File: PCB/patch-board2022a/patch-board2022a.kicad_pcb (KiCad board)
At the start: 2 copper layers, 230 x 63 mm, 120 parts, among them J1 USB_B, J10 SERVO POWER SUPPLY, J11 AOUT1, J12 AOUT2, J13 AOUT3, J14 AOUT4, J15 AOUT5, J16 AOUT6, J17 AOUT7, J18 AOUT8, J2 LOGIC POWER SUPPLY, J21 DIGITAL OUT1, J22 DIGITAL OUT2, J23 DIGITAL OUT3, J24 DIGITAL OUT4, J3 MEGA_13-8, J31 S01, J32 S02, J33 S03, J34 S04, J35 S05, J36 S06, J37 S07, J38 S08, J39 S09, J4 MEGA_7-0, J41 SV, J42 SV, J43 SV, J44 SV, J45 SV, J46 SV, J5 MEGA_14-21, J6 MEGA_A8-A15, J7 MEGA_A0-A7, J8 MEGA_POWER, J9 MEGA_22-53, SW1 D1A, SW11 SW_DPST, SW12 SW_DPST, SW13 Conn_01x02, SW2 D1B, SW3 D2A, SW4 D2B, SW5 D3A, SW6 D3B, SW7 D4A, SW8 D4B, U1 74HC00, U10 74HC08, U11 74HC00, U12 74HC08, U13 74HC08, U14 TLP785, U15 TLP785, U16 TLP785, U17 TLP785, U18 TLP785, U19 TLP785, U2 74HC08, U3 74HC08, U4 74HC00, U5 74HC08, U6 74HC08, U7 74HC14, U8 74HC00, U9 74HC08

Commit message: 一応完成
git-svn-id: https://shiro-home.ddns.net/svn/project/motor-driver/trunk@40 73406841-da20-4056-b287-c5b29fcc9b8e
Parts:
- removed J39: S09, Connector_PinHeader_2.54mm:PinHeader_1x03_P2.54mm_Vertical
- J11, J12, J13, J14, J15, J16, J17, J18: footprint Connector_PinHeader_2.54mm:PinHeader_1x02_P2.54mm_Vertical -> Connector_PinHeader_2.54mm:PinHeader_1x03_P2.54mm_Vertical
- J21: value DIGITAL OUT1 -> DOUT1; footprint Connector_PinHeader_2.54mm:PinHeader_1x02_P2.54mm_Vertical -> Connector_PinHeader_2.54mm:PinHeader_1x03_P2.54mm_Vertical
- J22: value DIGITAL OUT2 -> DOUT2; footprint Connector_PinHeader_2.54mm:PinHeader_1x02_P2.54mm_Vertical -> Connector_PinHeader_2.54mm:PinHeader_1x03_P2.54mm_Vertical
- J23: value DIGITAL OUT3 -> DOUT3; footprint Connector_PinHeader_2.54mm:PinHeader_1x02_P2.54mm_Vertical -> Connector_PinHeader_2.54mm:PinHeader_1x03_P2.54mm_Vertical
- J24: value DIGITAL OUT4 -> DOUT4; footprint Connector_PinHeader_2.54mm:PinHeader_1x02_P2.54mm_Vertical -> Connector_PinHeader_2.54mm:PinHeader_1x03_P2.54mm_Vertical
- moved R10 48.3 mm to (151.3, 69.5), turned to 0 degrees
- moved R9 43.3 mm to (151.3, 67.0), turned to 0 degrees
- moved R8 38.6 mm to (151.3, 64.4), turned to 0 degrees
- moved R7 34.2 mm to (151.3, 61.9), turned to 0 degrees
- moved R6 30.2 mm to (151.3, 59.4), turned to 0 degrees
- moved R5 26.8 mm to (151.3, 56.8), turned to 0 degrees
- moved R11 11.4 mm to (125.9, 82.2)
- moved R12 11.4 mm to (120.8, 82.2)
- moved R13 11.4 mm to (115.7, 82.2)
- moved R14 11.4 mm to (110.6, 82.2)
- moved R15 11.4 mm to (105.6, 82.2)
- moved R16 11.4 mm to (100.5, 82.2)
- moved U14 11.4 mm to (128.4, 61.9)
- moved U15 11.4 mm to (123.3, 61.9)
- moved U16 11.4 mm to (118.3, 61.9)
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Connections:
- J11 pad 2: /AOUT1A -> /AOUT1M
- J12 pad 2: /AOUT2A -> /AOUT2M
- J13 pad 2: /AOUT3A -> /AOUT3M
- J14 pad 2: /AOUT4A -> /AOUT4M
- J15 pad 2: /AOUT5A -> /AOUT5M
- J16 pad 2: /AOUT6A -> /AOUT6M
- J17 pad 2: /AOUT7A -> /AOUT7M
- J18 pad 2: /AOUT8A -> /AOUT8M
- J21 pad 1: /DOUT1A -> /DOUT1B
- J21 pad 2: /DOUT1B -> /DOUT1M
- J22 pad 1: /DOUT2A -> /DOUT2B
- J22 pad 2: /DOUT2B -> /DOUT2M
- J23 pad 1: /DOUT3A -> /DOUT3B
- J23 pad 2: /DOUT3B -> /DOUT3M
- J24 pad 1: /DOUT4A -> /DOUT4B
- J24 pad 2: /DOUT4B -> /DOUT4M
- J6 pad 1: Net-(J6-Pad1) -> /SENSOR1
- J6 pad 2: Net-(J6-Pad2) -> /SENSOR2
- J6 pad 3: Net-(J6-Pad3) -> /SENSOR3
- J6 pad 4: Net-(J6-Pad4) -> /SENSOR4
- J6 pad 5: Net-(J6-Pad5) -> /SENSOR5
- J6 pad 6: Net-(J6-Pad6) -> /SENSOR6
- J6 pad 7: Net-(J6-Pad7) -> /SENSOR7
- J6 pad 8: Net-(J6-Pad8) -> /SENSOR8
- J7 pad 1: Net-(J7-Pad1) -> /AOUT8M
- J7 pad 2: Net-(J7-Pad2) -> /AOUT7M
- J7 pad 3: Net-(J7-Pad3) -> /AOUT6M
- J7 pad 4: Net-(J7-Pad4) -> /AOUT5M
- J7 pad 5: Net-(J7-Pad5) -> /AOUT4M
- J7 pad 6: Net-(J7-Pad6) -> /AOUT3M
- J7 pad 7: Net-(J7-Pad7) -> /AOUT2M
- J7 pad 8: Net-(J7-Pad8) -> /AOUT1M
- J9 pad 10: /SENSOR8 -> /LED1
- J9 pad 11: /SENSOR3 -> /SV3IN
- J9 pad 12: /SENSOR9 -> /DIN1A
- J9 pad 13: /SENSOR4 -> /SV4IN
- J9 pad 14: /DIN1A -> /DIN1B
- J9 pad 15: /SENSOR5 -> /SV5IN
- J9 pad 16: /DIN1B -> /DIN2A
- J9 pad 17: /SENSOR6 -> /SV6IN
- J9 pad 18: /DIN2A -> /DIN2B
- J9 pad 19: /SV1IN -> Net-(J9-Pad19)
- J9 pad 20: /DIN2B -> /DIN3A
- J9 pad 21: /SV2IN -> Net-(J9-Pad21)
- J9 pad 22: /DIN3A -> /DIN3B
- J9 pad 23: /SV3IN -> Net-(J9-Pad23)
- J9 pad 24: /DIN3B -> /DIN4A
- J9 pad 25: /SV4IN -> Net-(J9-Pad25)
- J9 pad 26: /DIN4A -> /DIN4B
- J9 pad 27: /SV5IN -> Net-(J9-Pad27)
- J9 pad 28: /DIN4B -> /DOUT3M
- J9 pad 29: /SV6IN -> Net-(J9-Pad29)
- J9 pad 30: Net-(J9-Pad30) -> /DOUT4M
- J9 pad 5: /LED1 -> /SW12
- J9 pad 6: /SW12 -> /DOUT1M
- J9 pad 7: /SENSOR1 -> /SV1IN
- J9 pad 8: /SENSOR7 -> /DOUT2M
- J9 pad 9: /SENSOR2 -> /SV2IN
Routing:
- net /DOUT3M: track 0.00 -> 133.2 mm
- net /DOUT4M: track 0.00 -> 132.1 mm
- net /AOUT1M: track 0.00 -> 128.4 mm, vias 0 -> 2
- net /AOUT2M: track 0.00 -> 118.4 mm, vias 0 -> 2
- net /AOUT4M: track 0.00 -> 116.4 mm, vias 0 -> 2
- net /AOUT3M: track 0.00 -> 114.0 mm, vias 0 -> 2
- net /DOUT1M: track 0.00 -> 108.7 mm
- net /DOUT2M: track 0.00 -> 108.5 mm
- net GND: track 104.5 -> 2.58 mm, vias 34 -> 144
- net /AOUT5M: track 0.00 -> 75.9 mm
- net /SV6IN: track 74.7 -> 3.17 mm
- net /SV5IN: track 67.8 -> 3.17 mm
- net /AOUT6M: track 0.00 -> 62.6 mm
- net /SV4IN: track 60.9 -> 3.17 mm
- net /LED1: track 0.00 -> 54.1 mm, vias 0 -> 3
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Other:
- board text added: "1 28"
- board text added: "2 30"
- board text added: "3 32"
- board text added: "4 34"
- board text added: "5 36"
- board text added: "6 38"
- board text removed: "1 19"
- board text removed: "2 21"
- board text removed: "3 23"
- board text removed: "4 25"
- board text removed: "5 27"
- board text removed: "6 29"
- board text removed: "9 30"

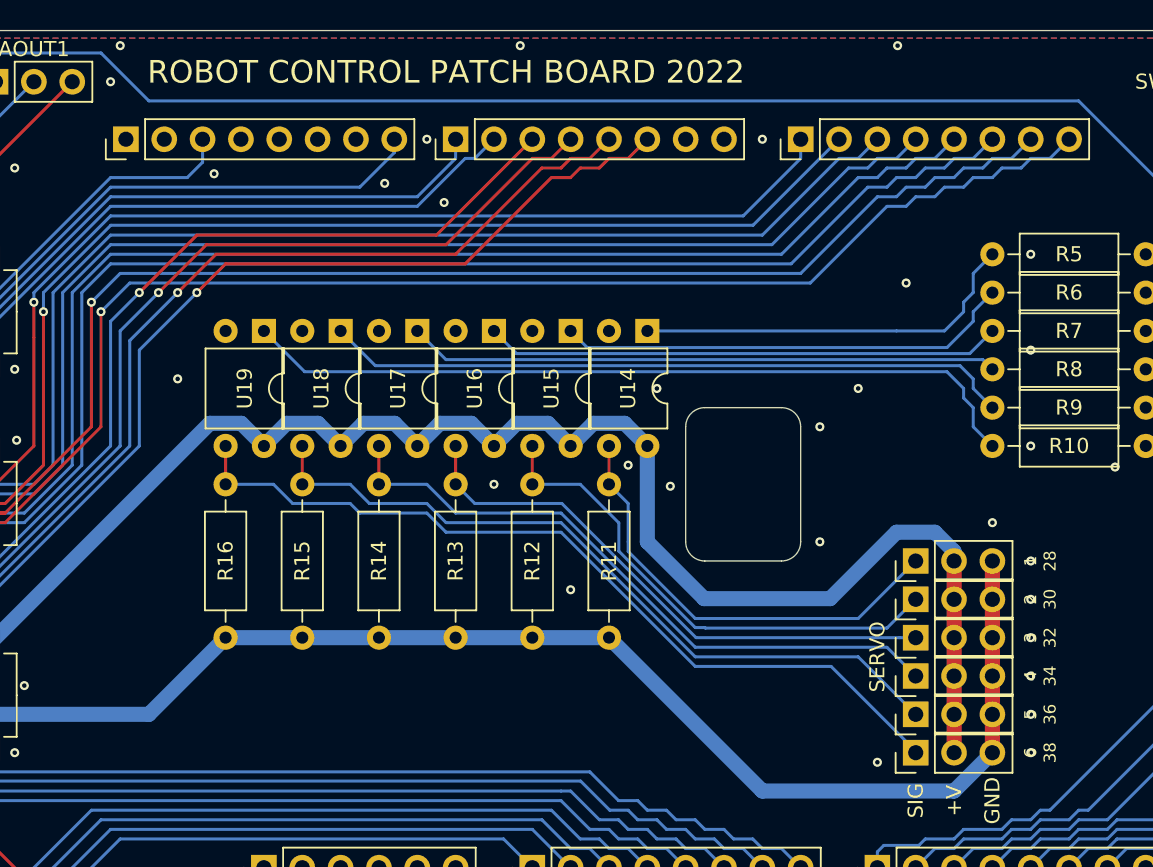
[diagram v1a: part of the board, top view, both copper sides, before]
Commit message: シルクが間違っていたのを修正
git-svn-id: https://shiro-home.ddns.net/svn/project/motor-driver/trunk@41 73406841-da20-4056-b287-c5b29fcc9b8e
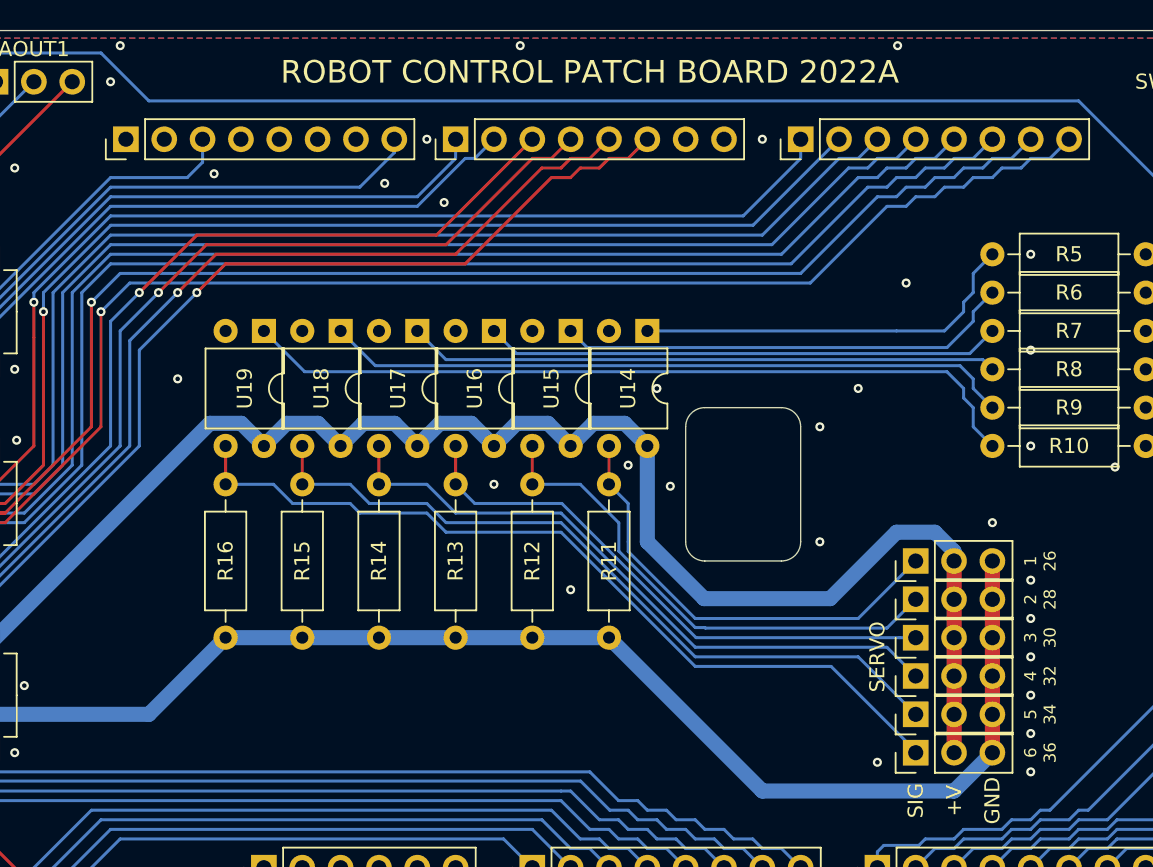
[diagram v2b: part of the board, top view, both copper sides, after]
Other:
- board text added: "1 26"
- board text added: "2 28"
- board text added: "3 30"
- board text added: "4 32"
- board text added: "5 34"
- board text added: "6 36"
- board text added: "ROBOT CONTROL PATCH BOARD 2022A"
- board text removed: "1 28"
- board text removed: "2 30"
- board text removed: "3 32"
- board text removed: "4 34"
- board text removed: "5 36"
- board text removed: "6 38"
- board text removed: "ROBOT CONTROL PATCH BOARD 2022"

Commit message: ガーバーデータを追加
git-svn-id: https://shiro-home.ddns.net/svn/project/motor-driver/trunk@46 73406841-da20-4056-b287-c5b29fcc9b8e
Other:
- rule pad_to_mask_clearance: 0.05 -> 0
